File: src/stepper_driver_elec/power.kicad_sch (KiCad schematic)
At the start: 35 parts, among them J210 XT30M, U220 MP2459GJ-Z-MS, U230 AP62200TWU, U240 HX4002

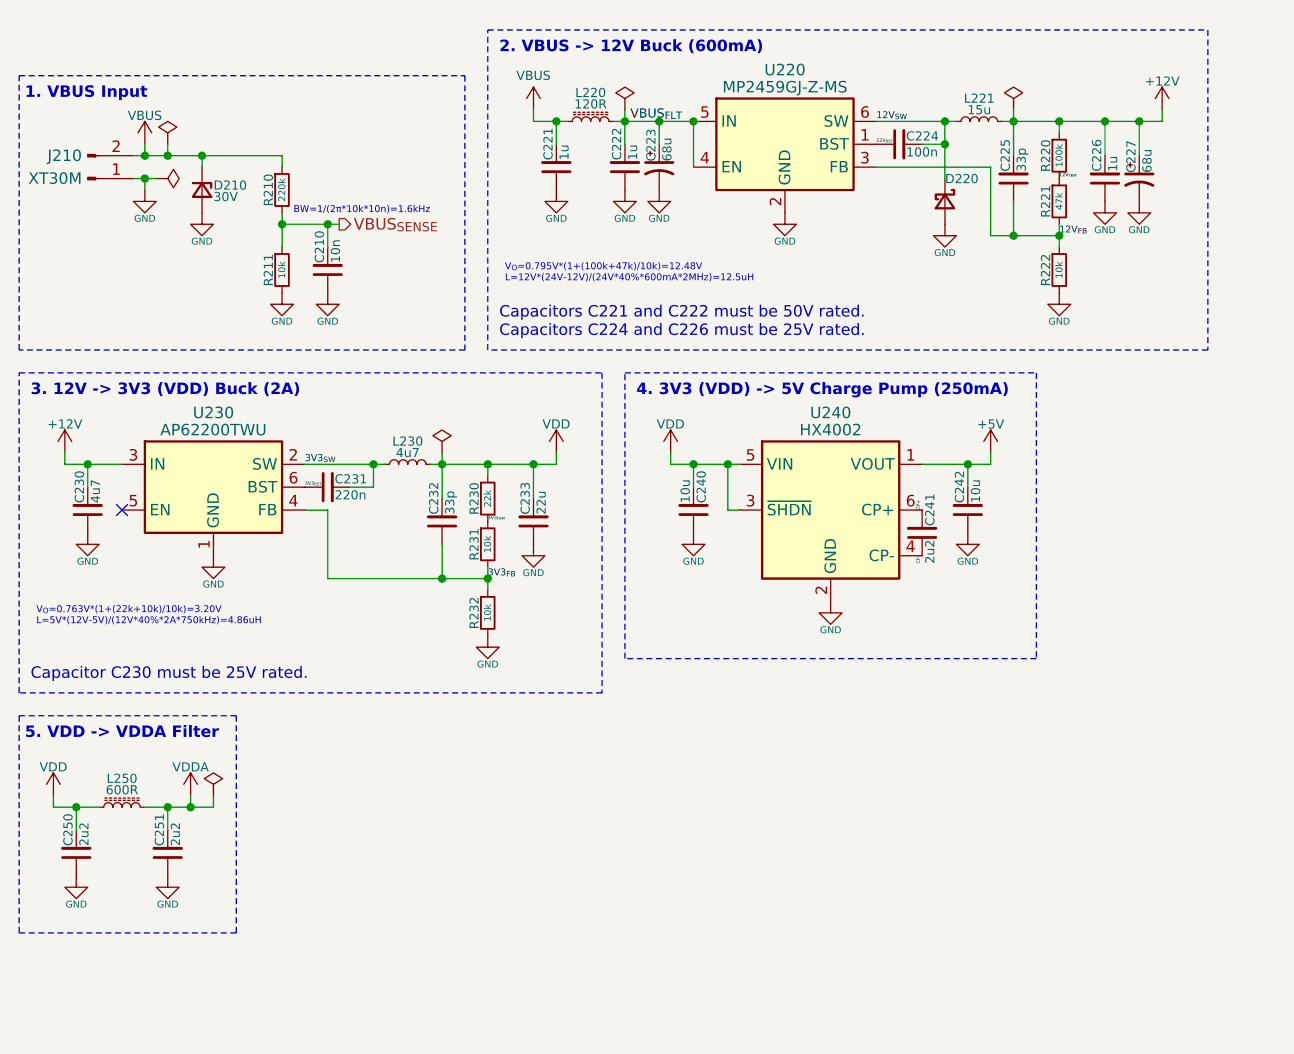
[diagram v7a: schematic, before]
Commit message: [ELEC] Stepper board v3.0 (#147)
* Significantly reduce the number of components based on testing data

* Before...

* fff

* Layout

* Silkscreen

* にゃー

* Clean up for production (purely cosmetic fixes save for shifting some vias slightly to the left for clearance)

* Fix JLC via complaint by changing all 0.3/0.4 mm vias to 0.3/0.45

---------

Co-authored-by: Jonah Hopkin <jonahhopkin@gmail.com>
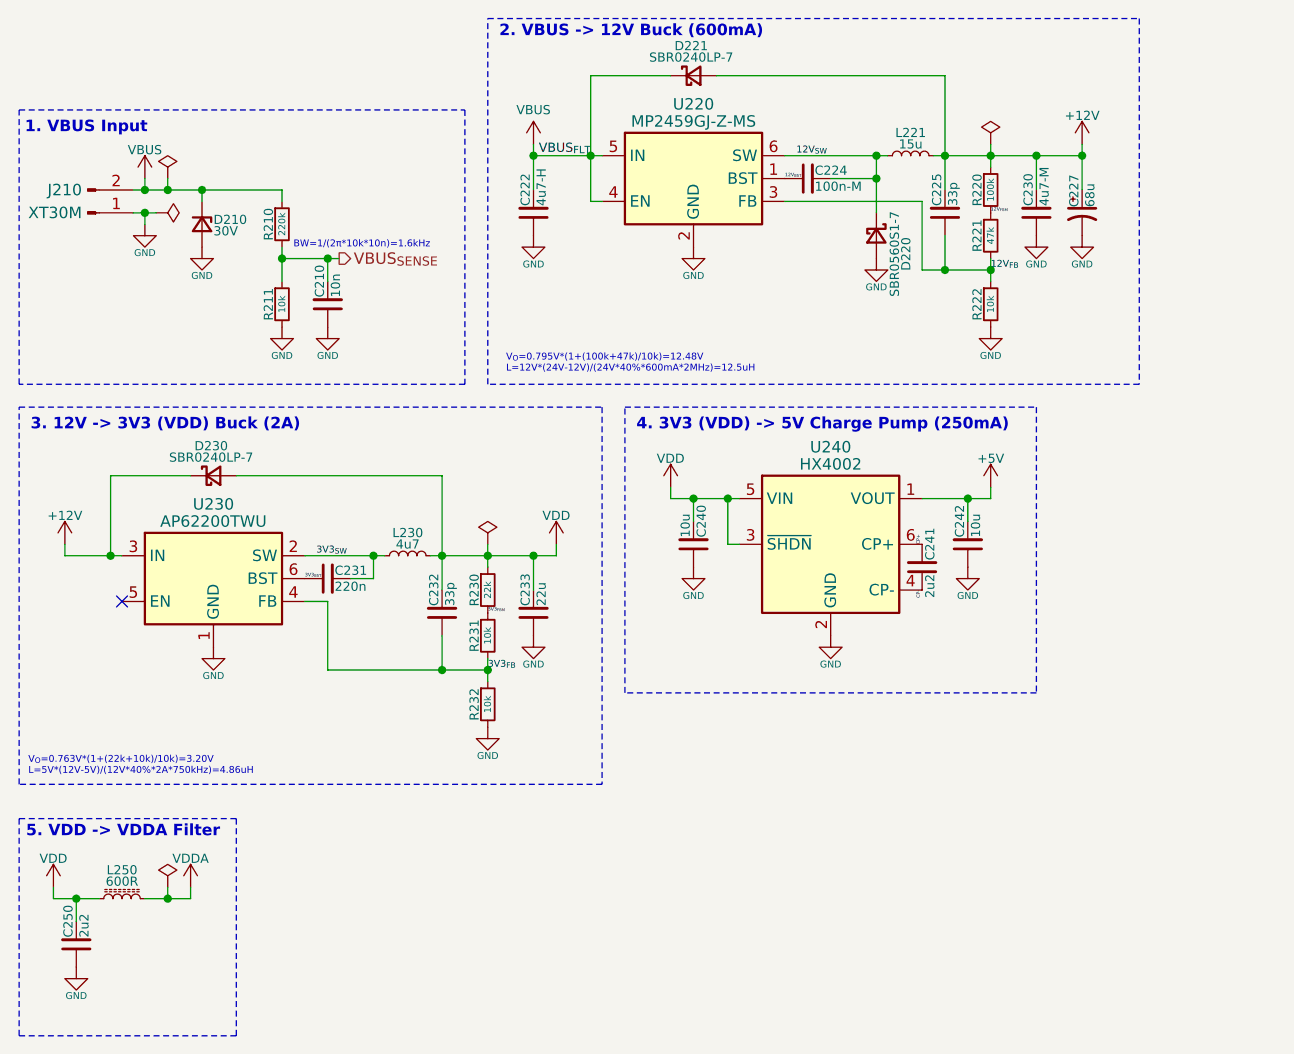
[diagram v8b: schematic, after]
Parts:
- removed C221: 1u, Capacitor_SMD:C_1206_3216Metric, symbol Bluesat:C_CompactV
- removed C223: 68u, Capacitor_SMD:CP_Elec_6.3x7.7, symbol Device:C_Polarized_Small_US
- removed C226: 1u, Capacitor_SMD:C_0805_2012Metric, symbol Bluesat:C_CompactV
- removed C251: 2u2, Capacitor_SMD:C_0603_1608Metric, symbol Bluesat:C_CompactV
- removed L220: 120R, Resistor_SMD:R_0603_1608Metric, symbol Device:L_Ferrite_Small
- added D221, D230: SBR0240LP-7, Diode_SMD:D_SOD-882, symbol Device:D_Schottky_Small
- C222: value 1u -> 4u7-H; footprint Capacitor_SMD:C_1206_3216Metric -> Capacitor_SMD:C_1210_3225Metric
- C224: value 100n -> 100n-M
- C230: value 4u7 -> 4u7-M
- D220: value D_Schottky_Small -> SBR0560S1-7
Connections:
- net VBUS_{FLT} is gone; now on net VBUS: C222.2, U220.4 (EN), U220.5 (IN)
- net +12V: now also D221.2 (A), D230.1 (K)
- net VBUS: now also D221.1 (K)
- net VDD: now also D230.2 (A)
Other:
- note removed: "Capacitor C230 must be 25V rated."
- note removed: "Capacitors C221 and C222 must be 50V rated. Capacitors C224 and C226 must be 25V rated."
- company: (none) -> Bluesat OWR
- title: (none) -> Stepper Motor Driver
- moved on the sheet: C210, C222, C224, C225, C227, C230, C231, C232, C233, C240, C241, C242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
